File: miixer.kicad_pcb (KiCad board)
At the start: 2 copper layers, 100 x 100 mm, 30 parts, among them J1 USB_C_Receptacle_USB2.0_16P, J2 Conn_01x10_Pin, SW2 SW_SPST, SW3 SW_SPST, SW4 SW_SPST, SW5 SW_SPST, SW6 SW_SPST, SW7 SW_SPST, SW8 SW_SPST, SW9 SW_SPST, U1 ESP32-C3-WROOM-02-N4, U2 ADS1115IDGS, U3 USBLC6-2SC6, U4 AP2127K-3.3, U5 PCF8574T

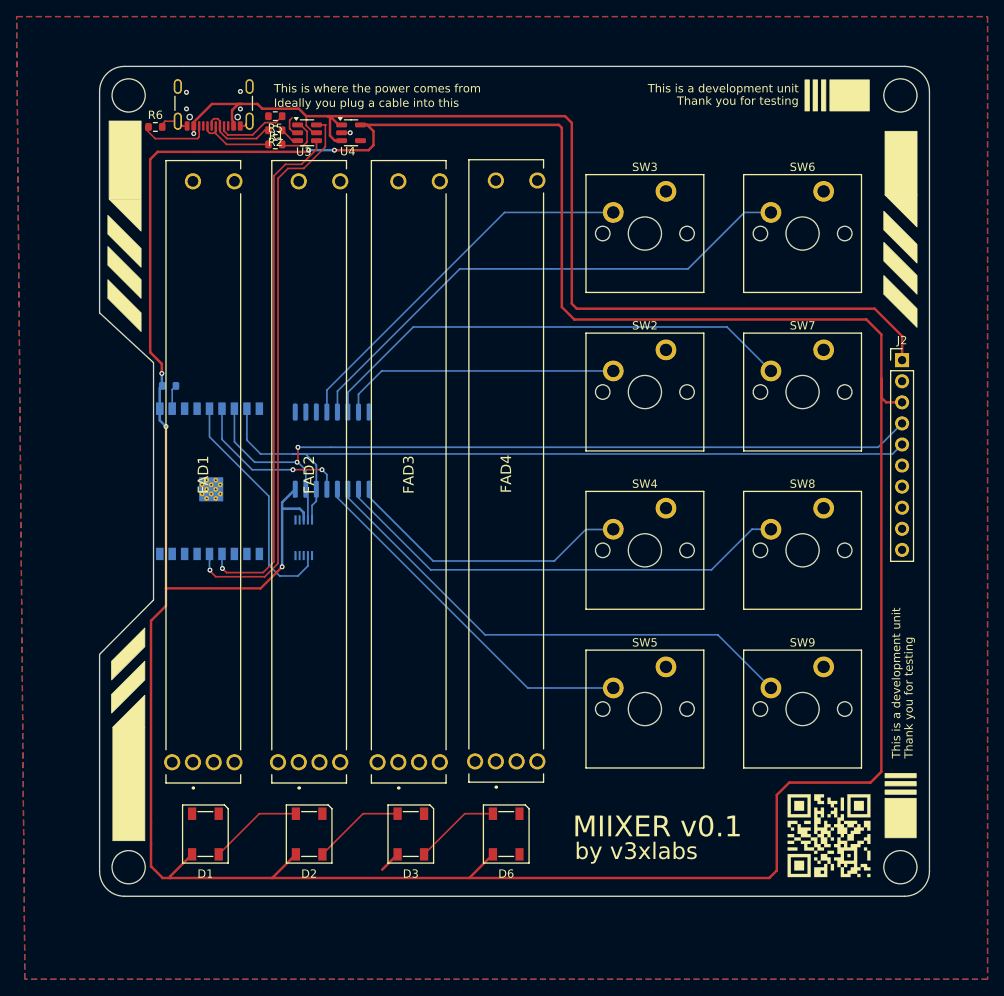
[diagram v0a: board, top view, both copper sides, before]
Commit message: Add LED driver ic TLC59208F
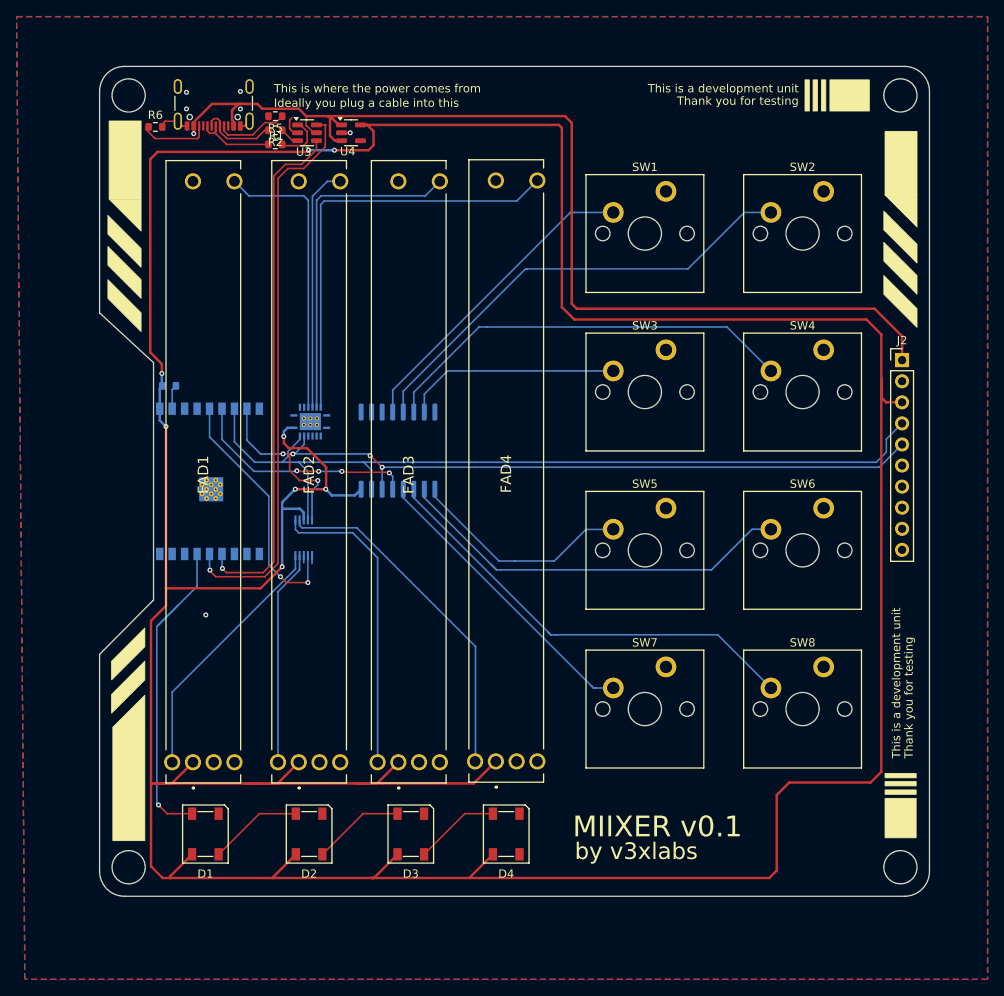
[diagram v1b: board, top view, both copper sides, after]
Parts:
- removed QR***** (x2): https://miixer.v3x.tools/_/pcb, 00_Luc:https___miixer.v3x.tools___pcb
- added U6: TLC59208FIRGYR, TLC59208FIRGYR:RGY16_2P55X2P05, B.Cu at (54.4, 69.8)
- U1: value ESP32-C3-WROOM-02-N4 -> ESP32-C3-WROOM-02
- moved U5 7.93 mm to (65.0, 73.3)
- renumbered D6 to D4, SW3 to SW1, SW6 to SW2, SW2 to SW3, SW7 to SW4, SW4 to SW5, SW8 to SW6, SW5 to SW7, SW9 to SW8
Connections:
- FAD1 pad 1: Net-(FAD1-CCW) -> +3.3V
- FAD1 pad 2: unconnected-(FAD1-WIPER-Pad2) -> /Buttons/FAD1_WIPER
- FAD1 pad 3: unconnected-(FAD1-CW-Pad3) -> GND
- FAD1 pad B1: Net-(FAD1-B_(+)) -> /Buttons/FAD1_LED
- FAD2 pad 1: Net-(FAD2-CCW) -> +3.3V
- FAD2 pad 2: unconnected-(FAD2-WIPER-Pad2) -> /Buttons/FAD2_WIPER
- FAD2 pad 3: unconnected-(FAD2-CW-Pad3) -> GND
- FAD2 pad B1: Net-(FAD2-B_(+)) -> /Buttons/FAD2_LED
- FAD3 pad 1: Net-(FAD3-CCW) -> +3.3V
- FAD3 pad 2: unconnected-(FAD3-WIPER-Pad2) -> /Buttons/FAD3_WIPER
- FAD3 pad 3: unconnected-(FAD3-CW-Pad3) -> GND
- FAD3 pad B1: Net-(FAD3-B_(+)) -> /Buttons/FAD3_LED
- FAD4 pad 1: Net-(FAD4-CCW) -> +3.3V
- FAD4 pad 2: unconnected-(FAD4-WIPER-Pad2) -> /Buttons/FAD4_WIPER
- FAD4 pad 3: unconnected-(FAD4-CW-Pad3) -> GND
- FAD4 pad B1: Net-(FAD4-B_(+)) -> /Buttons/FAD4_LED
- U1 pad 15: unconnected-(U1-IO3-Pad15) -> /Buttons/LED_MCU
- U2 pad 4: unconnected-(U2-AIN0-Pad4) -> /Buttons/FAD2_WIPER
- U2 pad 5: unconnected-(U2-AIN1-Pad5) -> /Buttons/FAD1_WIPER
- U2 pad 6: unconnected-(U2-AIN2-Pad6) -> /Buttons/FAD3_WIPER
- U2 pad 7: unconnected-(U2-AIN3-Pad7) -> /Buttons/FAD4_WIPER
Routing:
- net +3.3V: track 404.5 -> 488.4 mm, vias 5 -> 8
- net /Buttons/FAD4_LED: track 0.00 -> 51.7 mm
- net /Buttons/FAD4_WIPER: track 0.00 -> 41.8 mm
- net /Buttons/FAD3_LED: track 0.00 -> 40.7 mm
- net /Buttons/LED_MCU: track 0.00 -> 40.2 mm, vias 0 -> 1
- net /Buttons/FAD3_WIPER: track 0.00 -> 37.1 mm
- net /Buttons/FAD1_LED: track 0.00 -> 34.8 mm
- net /Buttons/FAD1_WIPER: track 0.00 -> 31.1 mm
- net /Buttons/FAD2_LED: track 0.00 -> 29.5 mm
- net /Buttons/FAD2_WIPER: track 0.00 -> 26.0 mm
- net Net-(SW4-A): track 58.8 -> 50.9 mm
- net Net-(SW5-A): track 35.1 -> 27.2 mm
- net Net-(SW3-A): track 34.0 -> 26.1 mm
- net Net-(SW2-A): track 63.7 -> 55.7 mm
- net Net-(SW1-A): track 46.0 -> 38.1 mm
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
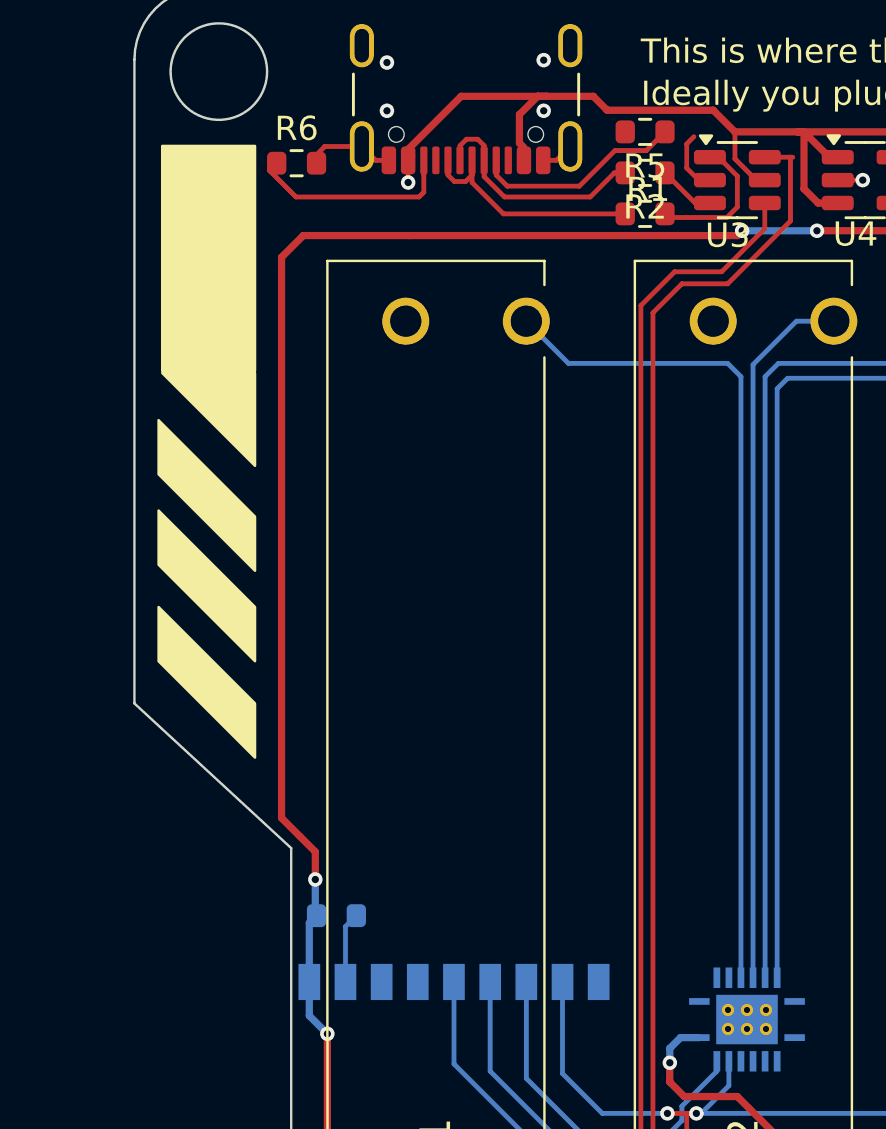
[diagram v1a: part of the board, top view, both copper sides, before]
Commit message: Add QWIIC connector
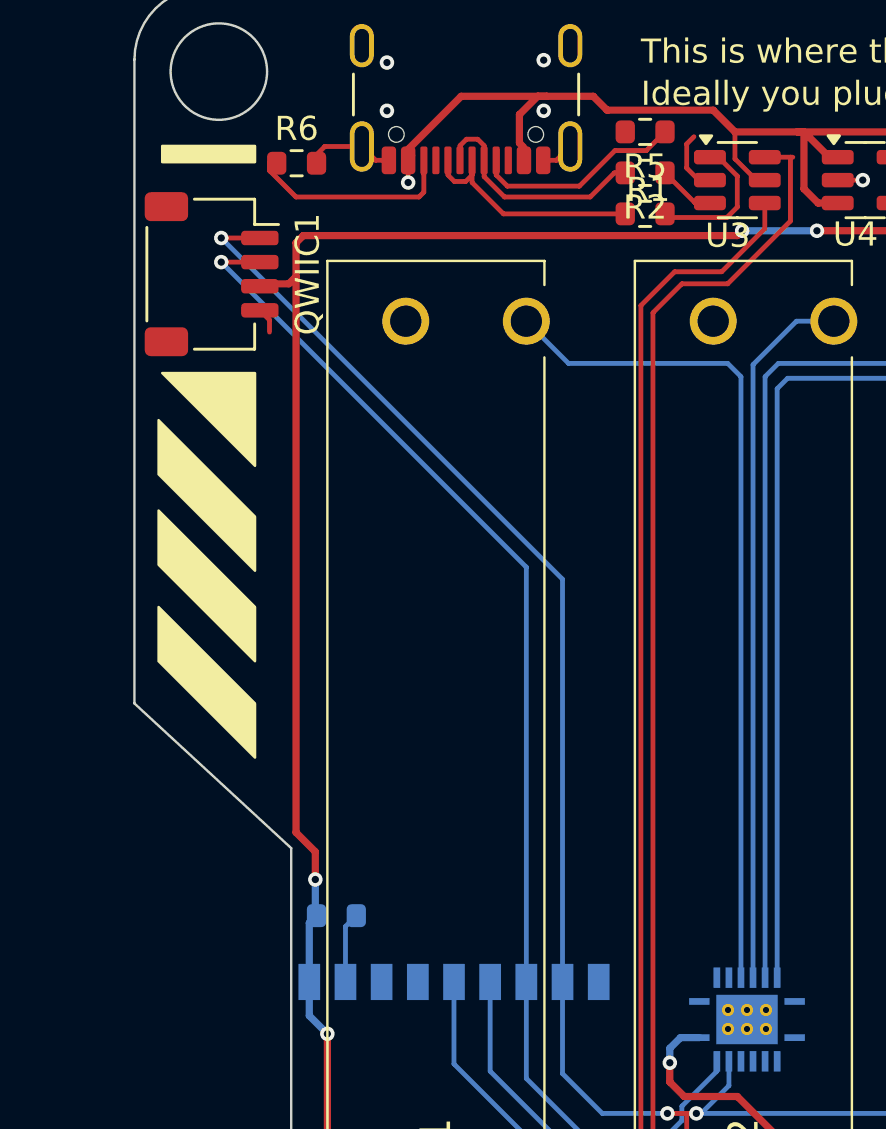
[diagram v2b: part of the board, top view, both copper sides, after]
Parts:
- added QWIIC1: Qwiic, Connector_JST:JST_SH_SM04B-SRSS-TB_1x04-1MP_P1.00mm_Horizontal, F.Cu at (32.2, 38.9)
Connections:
- U6 pad 10: unconnected-(U6-*OUT5-Pad10) -> /Buttons/EXTRA_LED_2
- U6 pad 11: unconnected-(U6-*OUT6-Pad11) -> /Buttons/EXTRA_LED_3
- U6 pad 12: unconnected-(U6-*OUT7-Pad12) -> /Buttons/EXTRA_LED_4
- U6 pad 9: unconnected-(U6-*OUT4-Pad9) -> /Buttons/EXTRA_LED_1
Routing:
- net /SCL: track 101.5 -> 139.8 mm, vias 5 -> 6
- net /SDA: track 103.6 -> 140.2 mm, vias 0 -> 1
- net +3.3V: track 488.4 -> 489.5 mm
- net GND: track 11.2 -> 12.2 mm

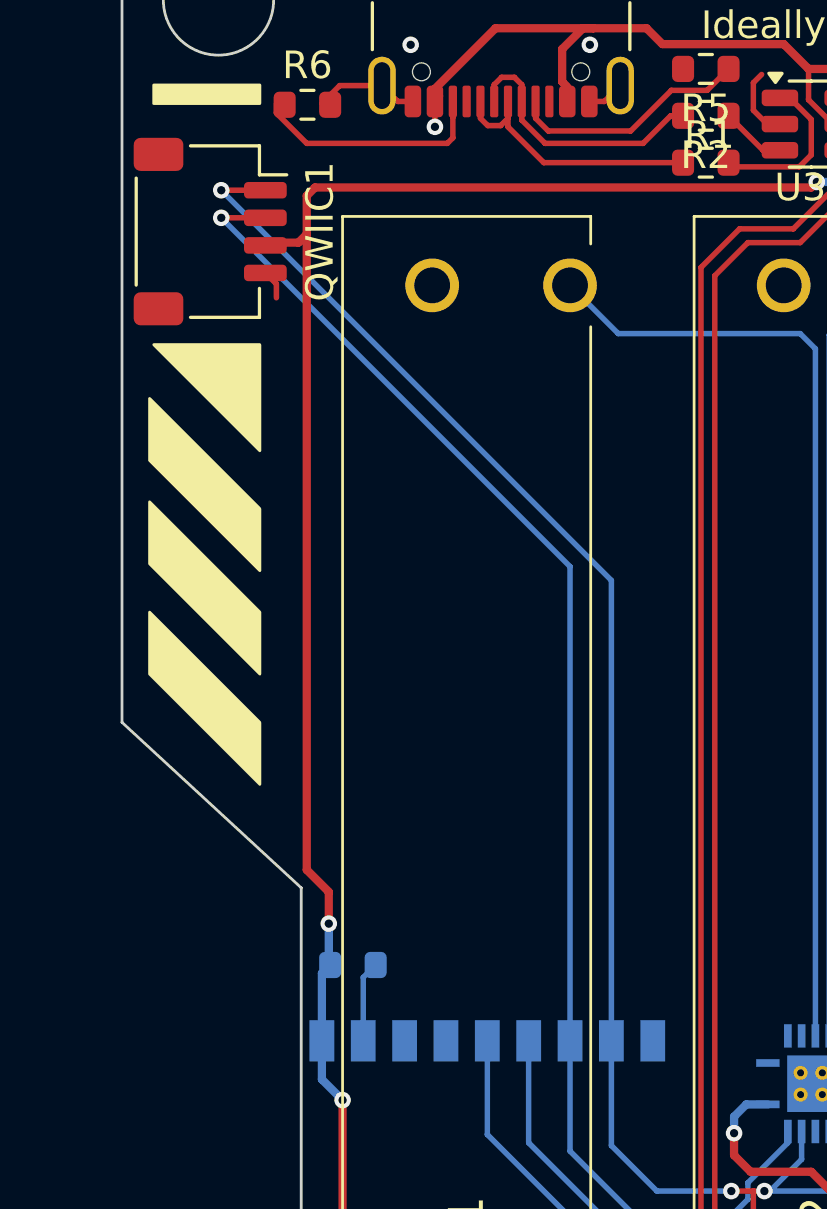
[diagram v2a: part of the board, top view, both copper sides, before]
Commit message: Update QWIIC connector
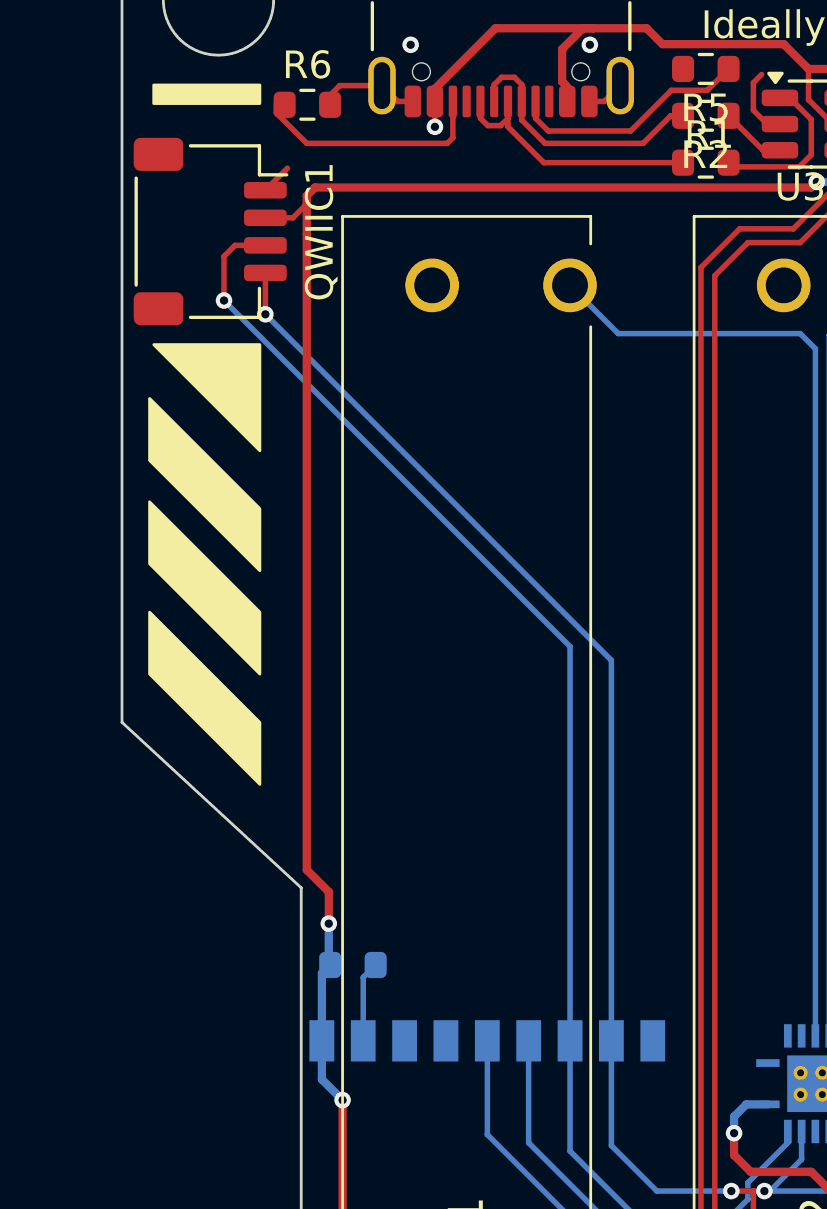
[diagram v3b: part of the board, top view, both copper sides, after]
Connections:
- QWIIC1 pad 1: /SCL -> GND
- QWIIC1 pad 2: /SDA -> +3.3V
- QWIIC1 pad 3: +3.3V -> /SDA
- QWIIC1 pad 4: GND -> /SCL
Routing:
- net /SCL: track 139.8 -> 134.5 mm
- net /SDA: track 140.2 -> 139.0 mm
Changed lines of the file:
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@@
 			(layers "F.Cu" "F.Mask" "F.Paste")
 			(roundrect_rratio 0.25)
-			(net 52 "/SCL")
+			(net 1 "GND")
 			(pinfunction "Pin_1")
 			(pintype "passive")
@@
 			(layers "F.Cu" "F.Mask" "F.Paste")
 			(roundrect_rratio 0.25)
-			(net 51 "/SDA")
+			(net 4 "+3.3V")
 			(pinfunction "Pin_2")
 			(pintype "passive")
@@
 			(layers "F.Cu" "F.Mask" "F.Paste")
 			(roundrect_rratio 0.25)
-			(net 4 "+3.3V")
+			(net 51 "/SDA")
 			(pinfunction "Pin_3")
 			(pintype "passive")
@@
 			(layers "F.Cu" "F.Mask" "F.Paste")
 			(roundrect_rratio 0.25)
-			(net 1 "GND")
+			(net 52 "/SCL")
 			(pinfunction "Pin_4")
 			(pintype "passive")
@@
 		(fp_text user "*"
 			(at -0.75 3.187342 90)
+			(unlocked yes)
 			(layer "B.SilkS")
 			(effects
@@
 		(fp_text user "*"
 			(at -0.75 3.187342 90)
-			(unlocked yes)
 			(layer "B.SilkS")
 			(effects
@@
 		(fp_text user "*"
 			(at -0.75 3.187342 90)
-			(unlocked yes)
 			(layer "B.Fab")
 			(effects
@@
 		(fp_text user "*"
 			(at -0.75 3.187342 90)
+			(unlocked yes)
 			(layer "B.Fab")
 			(effects
@@
 	)
 	(segment
-		(start 34.2 40.4)
-		(end 34.6 40.8)
-		(width 0.2)
-		(layer "F.Cu")
-		(net 1)
-	)
-	(segment
 		(start 39.005 34.18)
 		(end 38.43 33.605)
@@
 	)
 	(segment
-		(start 39.55 34.18)
-		(end 39.005 34.18)
+		(start 34.2 37.4)
+		(end 35 36.6)
 		(width 0.2)
 		(layer "F.Cu")
@@
 	)
 	(segment
-		(start 51.9 33.5)
-		(end 52.2 33.2)
+		(start 39.55 34.18)
+		(end 39.005 34.18)
 		(width 0.2)
 		(layer "F.Cu")
@@
 	)
 	(segment
-		(start 34.6 40.8)
-		(end 34.6 41.3)
+		(start 51.9 33.5)
+		(end 52.2 33.2)
 		(width 0.2)
 		(layer "F.Cu")
@@
 	)
 	(segment
-		(start 35.4 39.3)
-		(end 35.7 39)
-		(width 0.3)
-		(layer "F.Cu")
-		(net 4)
-	)
-	(segment
 		(start 109.7 124.8)
 		(end 61.8 124.8)
@@
 	)
 	(segment
-		(start 35.2 123.4)
-		(end 35.2 120.7)
+		(start 34.2 38.4)
+		(end 35.2 38.4)
+		(width 0.2)
+		(layer "F.Cu")
+		(net 4)
+	)
+	(segment
+		(start 35.2 38.4)
+		(end 35.7 37.9)
+		(width 0.2)
+		(layer "F.Cu")
+		(net 4)
+	)
+	(segment
+		(start 35.7 37.6)
+		(end 35.7 37.9)
 		(width 0.3)
 		(layer "F.Cu")
@@
 	)
 	(segment
-		(start 112.1 113.3)
-		(end 110.6 114.8)
+		(start 35.2 123.4)
+		(end 35.2 120.7)
 		(width 0.3)
 		(layer "F.Cu")
@@
 	)
 	(segment
-		(start 34.3 39.3)
-		(end 35.4 39.3)
+		(start 112.1 113.3)
+		(end 110.6 114.8)
 		(width 0.3)
 		(layer "F.Cu")
@@
 	)
 	(segment
-		(start 34.2 39.4)
-		(end 34.3 39.3)
-		(width 0.2)
-		(layer "F.Cu")
-		(net 4)
-	)
-	(segment
 		(start 62 36.5)
 		(end 61.4 37.1)
@@
 	)
 	(segment
-		(start 35.7 37.6)
+		(start 35.7 37.9)
 		(end 35.7 39)
 		(width 0.3)
@@
 	)
 	(segment
-		(start 34.2 38.4)
-		(end 32.6 38.4)
+		(start 34.2 39.4)
+		(end 34.3 39.3)
+		(width 0.2)
+		(layer "F.Cu")
+		(net 51)
+	)
+	(segment
+		(start 33.1 39.4)
+		(end 34.2 39.4)
+		(width 0.2)
+		(layer "F.Cu")
+		(net 51)
+	)
+	(segment
+		(start 32.7 39.8)
+		(end 33.1 39.4)
+		(width 0.2)
+		(layer "F.Cu")
+		(net 51)
+	)
+	(segment
+		(start 32.7 41.4)
+		(end 32.7 39.8)
 		(width 0.2)
 		(layer "F.Cu")
@@
 	)
 	(via
-		(at 32.6 38.4)
+		(at 32.7 41.4)
 		(size 0.6)
 		(drill 0.3)
@@
 	)
 	(segment
+		(start 32.7 41.4)
+		(end 45.25 53.95)
+		(width 0.2)
+		(layer "B.Cu")
+		(net 51)
+	)
+	(segment
 		(start 53 74.7)
 		(end 51 74.7)
@@
 	)
 	(segment
-		(start 45.25 51.05)
-		(end 32.6 38.4)
+		(start 45.25 53.95)
+		(end 45.25 68.25)
 		(width 0.2)
 		(layer "B.Cu")
@@
 	)
 	(segment
-		(start 45.25 68.25)
-		(end 45.25 51.05)
-		(width 0.2)
-		(layer "B.Cu")
-		(net 51)
-	)
-	(segment
 		(start 47.7 74.7)
 		(end 45.25 72.25)
@@
 	)
 	(segment
-		(start 34.2 37.4)
-		(end 32.6 37.4)
-		(width 0.2)
-		(layer "F.Cu")
-		(net 52)
-	)
-	(segment
 		(start 51.1 73.7)
 		(end 51.9 73.7)
@@
 	)
 	(segment
+		(start 34.2 40.4)
+		(end 34.2 41.9)
+		(width 0.2)
+		(layer "F.Cu")
+		(net 52)
+	)
+	(segment
 		(start 51.9 75.7)
 		(end 53.1 76.9)
@@
 	)
 	(via
-		(at 32.6 37.4)
+		(at 52.3 73.7)
 		(size 0.6)
 		(drill 0.3)
@@
 	)
 	(via
-		(at 52.3 73.7)
+		(at 61.6 73.9)
 		(size 0.6)
 		(drill 0.3)
@@
 	)
 	(via
-		(at 61.6 73.9)
+		(at 55.3 76.9)
 		(size 0.6)
 		(drill 0.3)
@@
 	)
 	(via
-		(at 55.3 76.9)
+		(at 63.05 75.3)
 		(size 0.6)
 		(drill 0.3)
@@
 	)
 	(via
-		(at 63.05 75.3)
+		(at 34.2 41.9)
 		(size 0.6)
 		(drill 0.3)
@@
 	)
 	(segment
-		(start 32.6 37.4)
-		(end 46.75 51.55)
+		(start 122.96 75.3)
+		(end 125.7 72.56)
 		(width 0.2)
 		(layer "B.Cu")
@@
 	)
 	(segment
-		(start 122.96 75.3)
-		(end 125.7 72.56)
+		(start 34.2 41.9)
+		(end 46.75 54.45)
 		(width 0.2)
 		(layer "B.Cu")
@@
 	)
 	(segment
-		(start 46.75 51.55)
+		(start 46.75 54.45)
 		(end 46.75 68.25)
 		(width 0.2)
